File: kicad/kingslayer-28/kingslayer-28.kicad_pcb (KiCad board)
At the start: 2 copper layers, 133 x 95 mm, 119 parts, among them IC1 STM32F303CCT7, IC2 IS31FL3731-QFLS2-TR, IC3 LM3940IMP-3.3_NOPB, J1 Conn_01x04_Pin, K1 KEYSW, K10 KEYSW, K11 KEYSW, K12 KEYSW, K13 KEYSW, K14 KEYSW, K15 KEYSW, K16 KEYSW, K17 KEYSW, K18 KEYSW, K19 KEYSW, K2 KEYSW, K20 KEYSW, K21 KEYSW, K22 KEYSW, K24 KEYSW, K25 KEYSW, K26 KEYSW, K27 KEYSW, K28 KEYSW, K3 KEYSW, K4 KEYSW, K5 KEYSW, K6 KEYSW, K7 KEYSW, K8 KEYSW, K9 KEYSW, SW1 SS12D07, X1 IC21008.000M30.0EE1B

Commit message: 3d model
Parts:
- USB1: footprint Type-C:USB_C_GCT_USB4085 -> custom:USB_C_GCT_USB4085

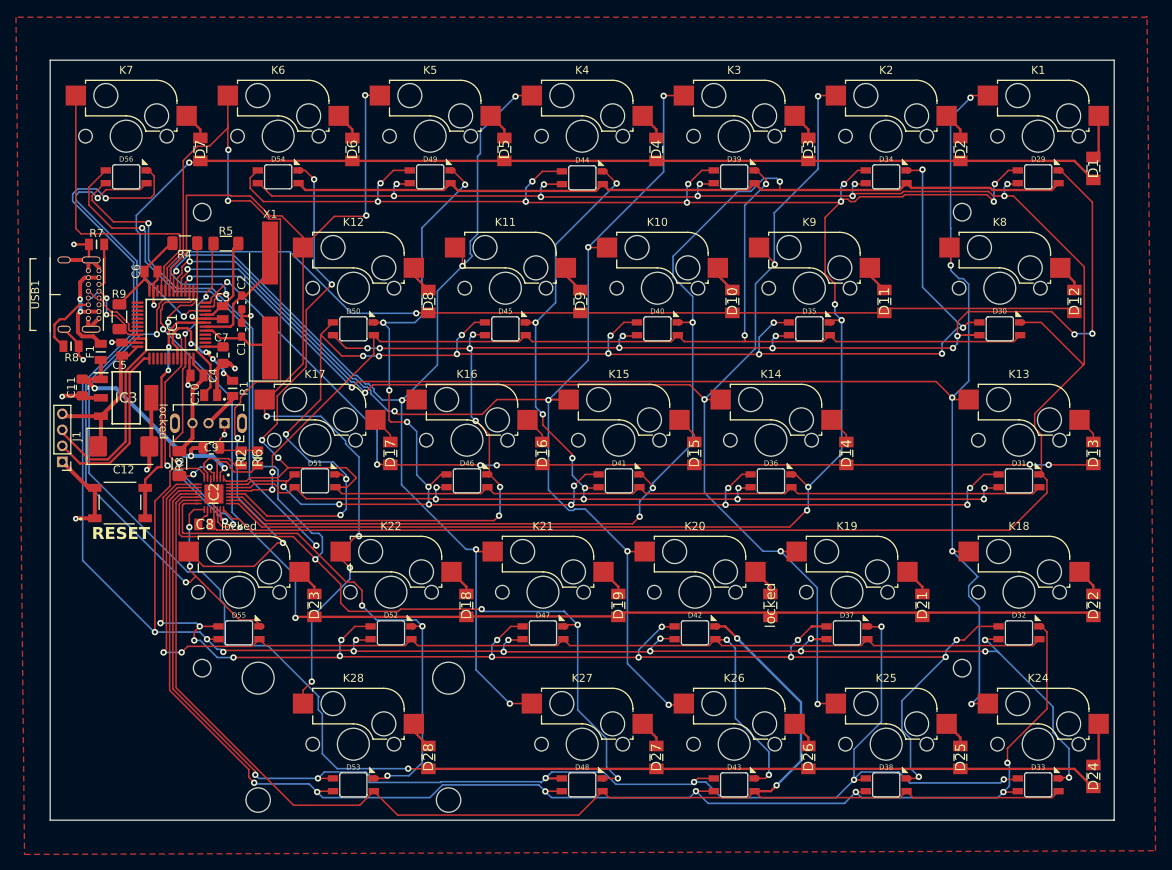
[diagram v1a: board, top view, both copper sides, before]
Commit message: Started DRC
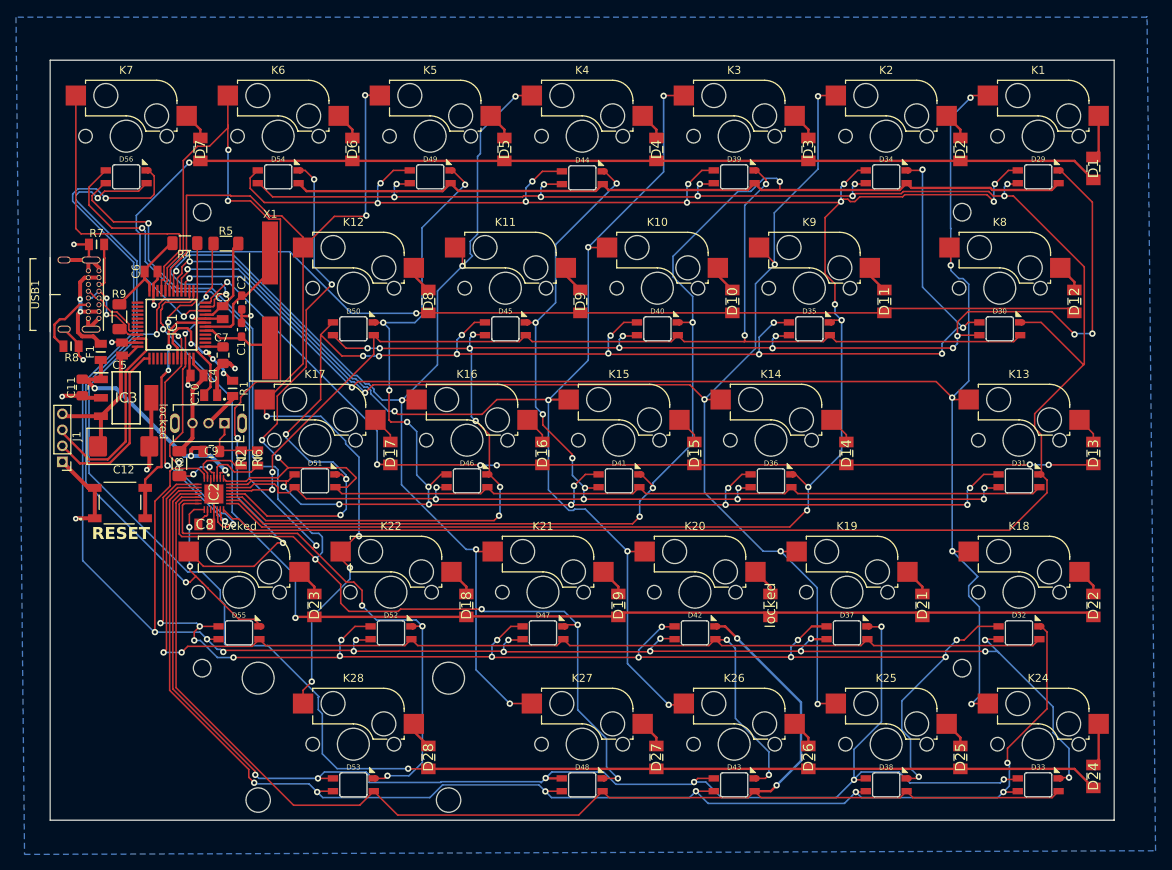
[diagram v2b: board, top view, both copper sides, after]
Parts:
- moved C9 0.43 mm to (99.7, 94.2)
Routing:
- net GND: track 88.0 -> 83.9 mm, vias 13 -> 11
- net ca4: track 195.0 -> 193.1 mm
- net cb2: track 180.8 -> 179.6 mm
- net +5V: track 33.0 -> 32.2 mm
- net sdb: track 8.11 -> 7.35 mm
- added copper zone on B.Cu, net GND
- removed copper zone on F.Cu, net GND

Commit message: finish DRC
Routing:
- net +3V3: track 60.2 -> 103.5 mm, vias 0 -> 10
- net cb1: track 252.6 -> 230.7 mm, vias 15 -> 18
- net ca3: track 210.4 -> 200.2 mm, vias 4 -> 6
- net cb5: track 174.0 -> 164.0 mm, vias 7 -> 4
- net cb9: track 92.1 -> 82.3 mm, vias 4 -> 7
- net row1: track 130.2 -> 139.2 mm
- net row3: track 151.7 -> 158.7 mm
- net cb4: track 174.5 -> 168.0 mm, vias 7 -> 12
- net cb6: track 176.9 -> 183.1 mm
- net ca8: track 170.8 -> 175.1 mm, vias 14 -> 19
- net cb3: track 159.6 -> 163.6 mm
- net cb8: track 131.3 -> 134.1 mm
- net row4: track 180.5 -> 182.6 mm, vias 2 -> 6
- net GND: track 83.9 -> 85.9 mm, vias 11 -> 12
- net +5V: track 32.2 -> 34.0 mm, vias 3 -> 5
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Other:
- board text added: "BOOT0"
- board text removed: "locked"

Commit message: found first error, need to redo pics and manufacturing
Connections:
- S1 pad 2: nrst -> GND
- S1 pad 3: GND -> nrst
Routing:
- net row4: track 182.6 -> 185.1 mm
- net cb9: track 82.3 -> 84.0 mm
- net nrst: track 41.0 -> 42.6 mm
- net cb1: track 230.7 -> 231.9 mm
- net GND: track 85.9 -> 86.7 mm, vias 12 -> 13

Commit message: ground loop
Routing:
- net cb1: track 231.9 -> 238.7 mm
- net cb9: track 84.0 -> 89.8 mm
- net row4: track 185.1 -> 190.2 mm
- net GND: track 86.7 -> 90.6 mm, vias 13 -> 12

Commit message: fix RGB
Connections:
- D29 pad 1: ca1 -> ca3
- D29 pad 2: ca2 -> ca4
- D29 pad 3: ca3 -> ca2
- D29 pad 4: ca4 -> ca1
- D30 pad 1: ca4 -> ca6
- D30 pad 2: ca5 -> ca1
- D30 pad 3: ca6 -> ca5
- D30 pad 4: ca1 -> ca4
- D31 pad 1: ca7 -> ca9
- D31 pad 2: ca8 -> ca1
- D31 pad 3: ca9 -> ca8
- D31 pad 4: ca1 -> ca7
- D32 pad 1: cb1 -> cb3
- D32 pad 2: cb2 -> cb4
- D32 pad 3: cb3 -> cb2
- D32 pad 4: cb4 -> cb1
- D33 pad 1: cb4 -> cb6
- D33 pad 2: cb5 -> cb1
- D33 pad 3: cb6 -> cb5
- D33 pad 4: cb1 -> cb4
- D34 pad 1: ca1 -> ca3
- D34 pad 2: ca2 -> ca5
- D34 pad 3: ca3 -> ca2
- D34 pad 4: ca5 -> ca1
- D35 pad 1: ca4 -> ca6
- D35 pad 2: ca5 -> ca2
- D35 pad 3: ca6 -> ca5
- D35 pad 4: ca2 -> ca4
- D36 pad 1: ca7 -> ca9
- D36 pad 2: ca8 -> ca2
- D36 pad 3: ca9 -> ca8
- D36 pad 4: ca2 -> ca7
- D37 pad 1: cb1 -> cb3
- D37 pad 2: cb2 -> cb5
- D37 pad 3: cb3 -> cb2
- D37 pad 4: cb5 -> cb1
- D38 pad 1: cb4 -> cb6
- D38 pad 2: cb5 -> cb2
- D38 pad 3: cb6 -> cb5
- D38 pad 4: cb2 -> cb4
- D39 pad 1: ca1 -> ca3
- D39 pad 2: ca2 -> ca6
- D39 pad 3: ca3 -> ca2
- D39 pad 4: ca6 -> ca1
- D40 pad 1: ca4 -> ca6
- D40 pad 2: ca5 -> ca3
- D40 pad 3: ca6 -> ca5
- D40 pad 4: ca3 -> ca4
- D41 pad 1: ca7 -> ca9
- D41 pad 2: ca8 -> ca3
- D41 pad 3: ca9 -> ca8
- D41 pad 4: ca3 -> ca7
- D42 pad 1: cb1 -> cb3
- D42 pad 2: cb2 -> cb6
- D42 pad 3: cb3 -> cb2
- D42 pad 4: cb6 -> cb1
- D43 pad 1: cb4 -> cb6
- D43 pad 2: cb5 -> cb3
- D43 pad 3: cb6 -> cb5
- D43 pad 4: cb3 -> cb4
- D44 pad 1: ca1 -> ca3
- D44 pad 2: ca2 -> ca7
- D44 pad 3: ca3 -> ca2
- D44 pad 4: ca7 -> ca1
- D45 pad 1: ca4 -> ca6
- D45 pad 2: ca5 -> ca7
- D45 pad 3: ca6 -> ca5
- D45 pad 4: ca7 -> ca4
- D46 pad 1: ca7 -> ca9
- D46 pad 2: ca8 -> ca4
- D46 pad 3: ca9 -> ca8
- D46 pad 4: ca4 -> ca7
- D47 pad 1: cb1 -> cb3
- D47 pad 2: cb2 -> cb7
- D47 pad 3: cb3 -> cb2
- D47 pad 4: cb7 -> cb1
- D48 pad 1: cb4 -> cb6
- D48 pad 2: cb5 -> cb7
- D48 pad 3: cb6 -> cb5
- D48 pad 4: cb7 -> cb4
- D49 pad 1: ca1 -> ca3
- D49 pad 2: ca2 -> ca8
- D49 pad 3: ca3 -> ca2
- D49 pad 4: ca8 -> ca1
- D50 pad 1: ca4 -> ca6
- D50 pad 2: ca5 -> ca8
- D50 pad 3: ca6 -> ca5
- D50 pad 4: ca8 -> ca4
- D51 pad 1: ca7 -> ca9
- D51 pad 2: ca8 -> ca5
- D51 pad 3: ca9 -> ca8
- D51 pad 4: ca5 -> ca7
- D52 pad 1: cb1 -> cb3
- D52 pad 2: cb2 -> cb8
- D52 pad 3: cb3 -> cb2
- D52 pad 4: cb8 -> cb1
- D53 pad 1: cb4 -> cb6
- D53 pad 2: cb5 -> cb8
- D53 pad 3: cb6 -> cb5
- D53 pad 4: cb8 -> cb4
- D54 pad 1: ca1 -> ca3
- D54 pad 2: ca2 -> ca9
- D54 pad 3: ca3 -> ca2
- D54 pad 4: ca9 -> ca1
- D55 pad 1: cb1 -> cb3
- D55 pad 2: cb2 -> cb9
- D55 pad 3: cb3 -> cb2
- D55 pad 4: cb9 -> cb1
- D56 pad 1: cb7 -> cb9
- D56 pad 2: cb8 -> cb1
- D56 pad 3: cb9 -> cb8
- D56 pad 4: cb1 -> cb7
- IC2 pad 3: sdb -> +5V
- R6 pad 1: sdb -> +5V
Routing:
- net ca7: track 156.4 -> 190.8 mm
- net cb5: track 164.0 -> 196.5 mm, vias 4 -> 12
- net ca1: track 272.6 -> 297.4 mm, vias 10 -> 12
- net ca8: track 175.1 -> 199.0 mm, vias 19 -> 20
- net cb4: track 168.0 -> 190.7 mm, vias 12 -> 17
- net ca3: track 200.2 -> 219.0 mm
- net cb1: track 238.7 -> 256.6 mm, vias 18 -> 20
- net cb3: track 163.6 -> 174.4 mm
- net ca4: track 193.1 -> 203.1 mm
- net ca2: track 250.2 -> 259.6 mm, vias 14 -> 16
- net cb6: track 183.1 -> 173.8 mm
- net cb2: track 179.8 -> 188.9 mm, vias 15 -> 17
- net sdb: track 7.35 -> 0.00 mm
- net cb8: track 134.1 -> 140.7 mm
- net cb7: track 155.3 -> 160.8 mm
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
